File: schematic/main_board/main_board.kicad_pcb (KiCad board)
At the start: 2 copper layers, 13 parts, among them J1 Line OUT, J2 Line IN, P1 +Vref, P2 GND, P3 -Vref, P4 Probe, P5 GND, U1 LM324N

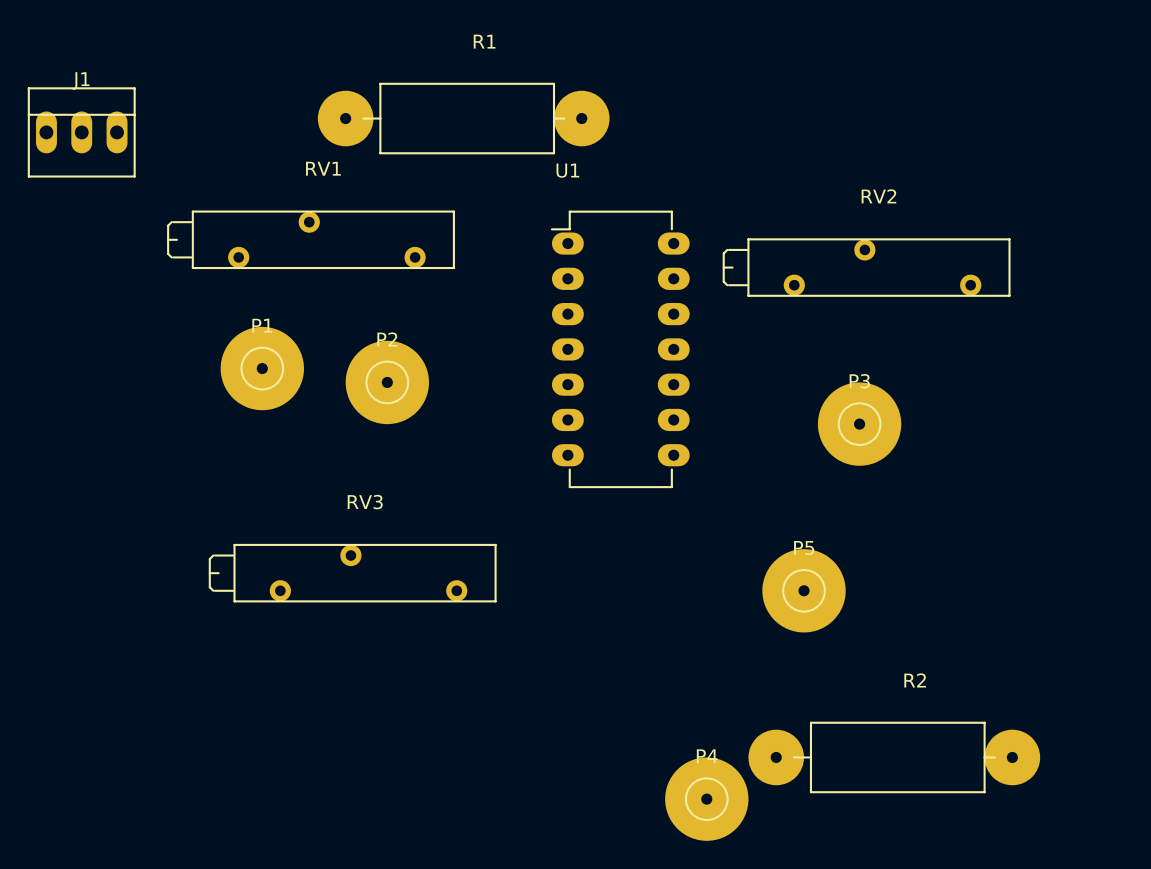
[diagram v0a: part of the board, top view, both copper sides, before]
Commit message: Trace route some wires on PCB.
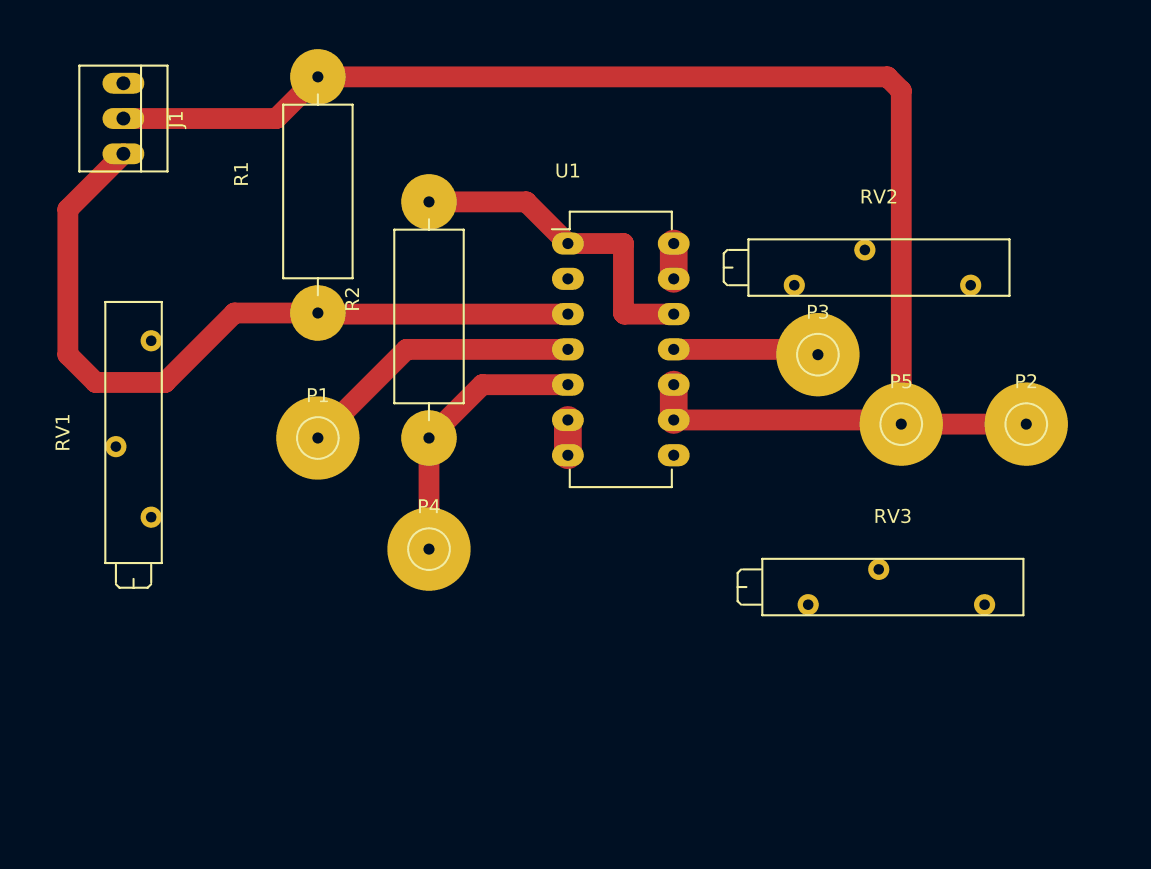
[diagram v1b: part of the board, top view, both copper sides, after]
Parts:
- moved P2 46.1 mm to (181.0, 89.0)
- moved RV3 38.0 mm to (178.0, 102.0)
- moved R2 34.0 mm to (138.0, 90.0), turned to 90 degrees
- moved P4 26.9 mm to (138.0, 98.0)
- moved RV1 19.9 mm to (118.0, 83.0), turned to 90 degrees
- moved R1 14.1 mm to (130.0, 81.0), turned to 90 degrees
- moved P5 13.9 mm to (172.0, 89.0)
- moved P1 6.40 mm to (130.0, 90.0)
- moved P3 5.83 mm to (166.0, 84.0)
- moved J1 3.16 mm to (116.0, 67.0), turned to 270 degrees
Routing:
- net GND: track 0.00 -> 109.7 mm
- net Net-(J1-Pad3): track 0.00 -> 55.0 mm
- net Net-(R2-Pad2): track 0.00 -> 23.9 mm
- net +12V: track 0.00 -> 20.6 mm
- net Net-(P4-Pad1): track 0.00 -> 19.6 mm
- net -12V: track 0.00 -> 10.5 mm
- net Net-(RV2-Pad1): track 0.00 -> 2.54 mm
- net Net-(RV3-Pad1): track 0.00 -> 2.54 mm
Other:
- net class Default: clearance 0.2 -> 0.5; trace_width 0.25 -> 1.5
- rule trace_clearance: 0.2 -> 0.5

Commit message: Add footprint for potentiometer.
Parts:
- RV1, RV2, RV3: footprint Potentiometers:Potentiometer_Bourns_3005_Angular_ScrewFront -> footprints:Potentiometer_CP3-36
- moved RV1 26.5 mm to (123.0, 109.0)
- moved RV2 20.1 mm to (186.0, 61.0)
- moved RV3 10.0 mm to (186.0, 108.0)

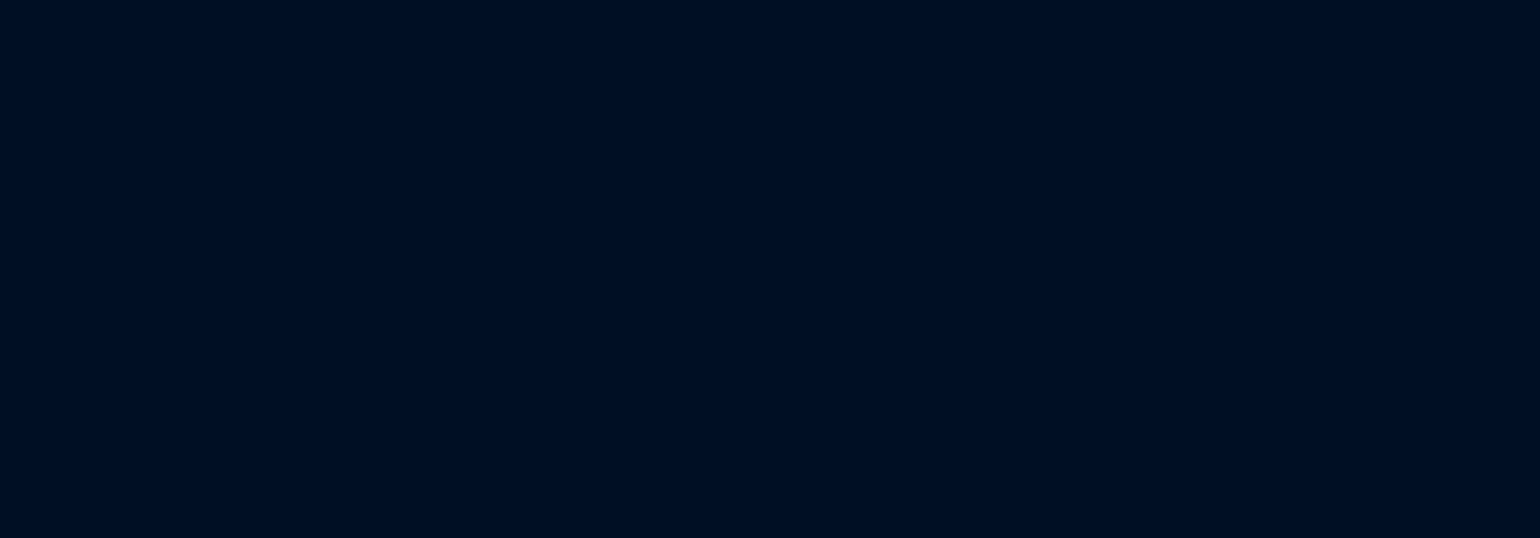
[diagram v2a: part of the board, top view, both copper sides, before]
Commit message: Added circuit to schematic for limit output voltage range.
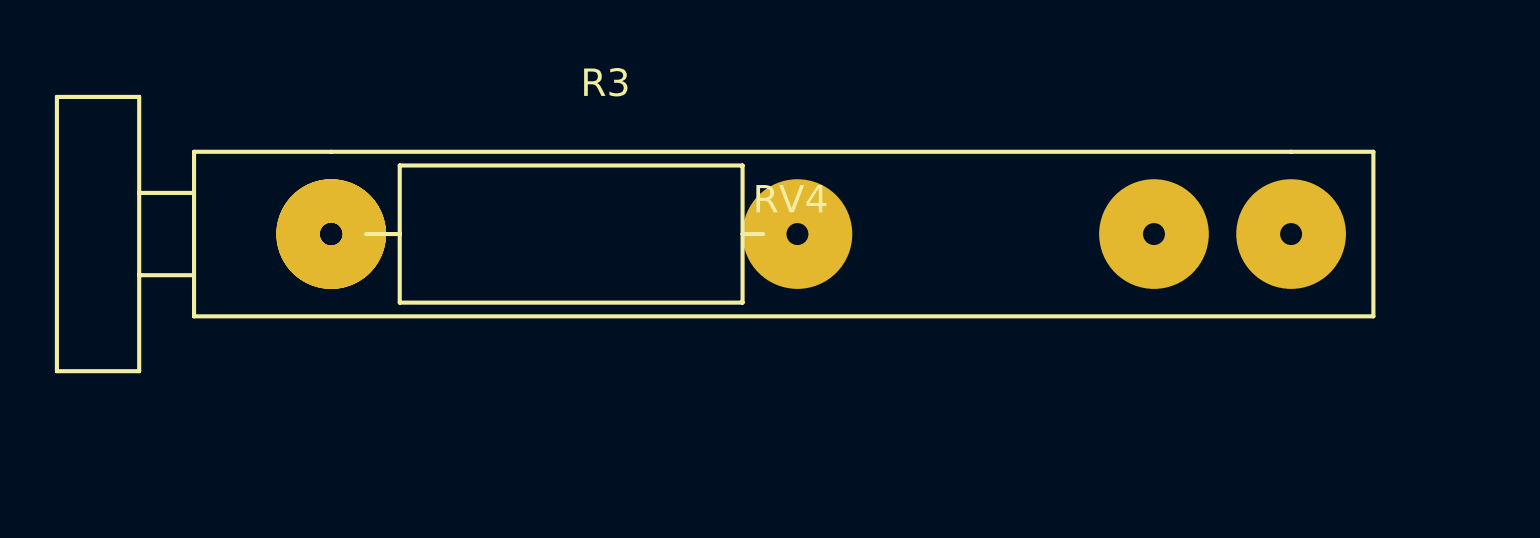
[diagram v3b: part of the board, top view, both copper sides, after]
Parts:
- added R3: 1k, footprints:Resistor_Horizontal_RM20mm_0.25W, F.Cu at (0.00, 0.00)
- added RV4: 100k, footprints:Potentiometer_CP3-36, F.Cu at (0.00, 0.00)
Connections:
- RV2 pad 1: Net-(RV2-Pad1) -> GND
- RV2 pad 3: GND -> Net-(RV2-Pad3)
- RV3 pad 1: Net-(RV3-Pad1) -> GND
- RV3 pad 3: GND -> Net-(RV3-Pad3)
- U1 pad 10: GND -> Net-(J1-Pad3)
- U1 pad 13: Net-(RV2-Pad1) -> Net-(RV2-Pad3)
- U1 pad 14: Net-(RV2-Pad1) -> Net-(RV2-Pad3)
- U1 pad 6: Net-(RV3-Pad1) -> Net-(RV3-Pad3)
- U1 pad 7: Net-(RV3-Pad1) -> Net-(RV3-Pad3)
- U1 pad 9: GND -> Net-(RV4-Pad2)
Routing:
- net GND: track 109.7 -> 91.1 mm
- net Net-(RV4-Pad2): track 0.00 -> 16.1 mm
- net Net-(RV2-Pad3): track 0.00 -> 2.54 mm
- net Net-(RV2-Pad1): track 2.54 -> 0.00 mm
- net Net-(J1-Pad3): track 55.0 -> 57.6 mm
- net Net-(RV3-Pad3): track 0.00 -> 2.54 mm
- net Net-(RV3-Pad1): track 2.54 -> 0.00 mm
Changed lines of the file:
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@@
 (kicad_pcb (version 4) (host pcbnew 4.0.2+e4-6225~38~ubuntu14.04.1-stable)
   (general
-    (links 25)
-    (no_connects 10)
+    (links 27)
+    (no_connects 14)
     (area 0 0 0 0)
     (thickness 1.6)
@@
     (tracks 32)
     (zones 0)
-    (modules 13)
-    (nets 14)
+    (modules 15)
+    (nets 17)
   )
   (page A4)
@@
   (net 9 "Net-(R2-Pad2)")
   (net 10 "Net-(RV1-Pad2)")
-  (net 11 "Net-(RV2-Pad1)")
-  (net 12 "Net-(RV3-Pad1)")
-  (net 13 "Net-(U1-Pad8)")
+  (net 11 "Net-(C1-Pad1)")
+  (net 12 "Net-(D2-Pad2)")
+  (net 13 "Net-(RV2-Pad3)")
+  (net 14 "Net-(RV3-Pad3)")
+  (net 15 "Net-(D1-Pad2)")
+  (net 16 "Net-(RV4-Pad2)")
   (net_class Default "This is the default net class."
     (clearance 0.5)
@@
     (add_net -12V)
     (add_net GND)
+    (add_net "Net-(C1-Pad1)")
+    (add_net "Net-(D1-Pad2)")
+    (add_net "Net-(D2-Pad2)")
     (add_net "Net-(J1-Pad1)")
     (add_net "Net-(J1-Pad3)")
@@
     (add_net "Net-(R2-Pad2)")
     (add_net "Net-(RV1-Pad2)")
-    (add_net "Net-(RV2-Pad1)")
-    (add_net "Net-(RV3-Pad1)")
-    (add_net "Net-(U1-Pad8)")
+    (add_net "Net-(RV2-Pad3)")
+    (add_net "Net-(RV3-Pad3)")
+    (add_net "Net-(RV4-Pad2)")
   )
   (module Connect:PINHEAD1-3 (layer F.Cu)
@@
       (net 8 "Net-(P4-Pad1)"))
     (pad 6 thru_hole oval (at 0 12.7) (size 2.3 1.6) (drill 0.8) (layers *.Cu *.Mask F.SilkS)
-      (net 12 "Net-(RV3-Pad1)"))
+      (net 14 "Net-(RV3-Pad3)"))
     (pad 7 thru_hole oval (at 0 15.24) (size 2.3 1.6) (drill 0.8) (layers *.Cu *.Mask F.SilkS)
-      (net 12 "Net-(RV3-Pad1)"))
+      (net 14 "Net-(RV3-Pad3)"))
     (pad 8 thru_hole oval (at 7.62 15.24) (size 2.3 1.6) (drill 0.8) (layers *.Cu *.Mask F.SilkS)
-      (net 13 "Net-(U1-Pad8)"))
+      (net 15 "Net-(D1-Pad2)"))
     (pad 9 thru_hole oval (at 7.62 12.7) (size 2.3 1.6) (drill 0.8) (layers *.Cu *.Mask F.SilkS)
-      (net 2 GND))
+      (net 16 "Net-(RV4-Pad2)"))
     (pad 10 thru_hole oval (at 7.62 10.16) (size 2.3 1.6) (drill 0.8) (layers *.Cu *.Mask F.SilkS)
-      (net 2 GND))
+      (net 3 "Net-(J1-Pad3)"))
     (pad 11 thru_hole oval (at 7.62 7.62) (size 2.3 1.6) (drill 0.8) (layers *.Cu *.Mask F.SilkS)
       (net 7 -12V))
@@
       (net 9 "Net-(R2-Pad2)"))
     (pad 13 thru_hole oval (at 7.62 2.54) (size 2.3 1.6) (drill 0.8) (layers *.Cu *.Mask F.SilkS)
-      (net 11 "Net-(RV2-Pad1)"))
+      (net 13 "Net-(RV2-Pad3)"))
     (pad 14 thru_hole oval (at 7.62 0) (size 2.3 1.6) (drill 0.8) (layers *.Cu *.Mask F.SilkS)
-      (net 11 "Net-(RV2-Pad1)"))
+      (net 13 "Net-(RV2-Pad3)"))
     (model Housings_DIP.3dshapes/DIP-14_W7.62mm_LongPads.wrl
       (at (xyz 0 0 0))
@@
     (fp_line (start -5 -3) (end 0 -3) (layer F.SilkS) (width 0.15))
     (pad 3 thru_hole circle (at 30 0) (size 4 4) (drill 0.8) (layers *.Cu *.Mask F.SilkS)
-      (net 2 GND))
+      (net 13 "Net-(RV2-Pad3)"))
     (pad 2 thru_hole circle (at 35 0) (size 4 4) (drill 0.8) (layers *.Cu *.Mask F.SilkS)
       (net 4 "Net-(J2-Pad1)"))
     (pad 1 thru_hole circle (at 0 0) (size 4 4) (drill 0.8) (layers *.Cu *.Mask F.SilkS)
-      (net 11 "Net-(RV2-Pad1)"))
+      (net 2 GND))
     (model Potentiometers.3dshapes/Potentiometer_Bourns_3005_Angular_ScrewFront.wrl
       (at (xyz 0 0 0))
@@
     (fp_line (start -5 -3) (end 0 -3) (layer F.SilkS) (width 0.15))
     (pad 3 thru_hole circle (at 30 0) (size 4 4) (drill 0.8) (layers *.Cu *.Mask F.SilkS)
-      (net 2 GND))
+      (net 14 "Net-(RV3-Pad3)"))
     (pad 2 thru_hole circle (at 35 0) (size 4 4) (drill 0.8) (layers *.Cu *.Mask F.SilkS)
       (net 5 "Net-(J2-Pad3)"))
     (pad 1 thru_hole circle (at 0 0) (size 4 4) (drill 0.8) (layers *.Cu *.Mask F.SilkS)
-      (net 12 "Net-(RV3-Pad1)"))
+      (net 2 GND))
+    (model Potentiometers.3dshapes/Potentiometer_Bourns_3005_Angular_ScrewFront.wrl
+      (at (xyz 0 0 0))
+      (scale (xyz 1 1 1))
+      (rotate (xyz 0 0 0))
+    )
+  )
+  (module footprints:Resistor_Horizontal_RM20mm_0.25W (layer F.Cu)
+    (at 0 0)
+    (descr "Resistor, Axial, RM 20mm,")
+    (tags "Resistor Axial RM 20mm")
+    (fp_text reference R3 (at 10 -5.4991) (layer F.SilkS)
+      (effects (font (size 1 1) (thickness 0.15)))
+    )
+    (fp_text value 1k (at 10 5.00126) (layer F.Fab)
+      (effects (font (size 1 1) (thickness 0.15)))
+    )
+    (fp_line (start 15 0) (end 15.75 0) (layer F.SilkS) (width 0.15))
+    (fp_line (start 2.5 0) (end 2.5 -2.5) (layer F.SilkS) (width 0.15))
+    (fp_line (start 2.5 -2.5) (end 15 -2.5) (layer F.SilkS) (width 0.15))
+    (fp_line (start 15 -2.5) (end 15 2.5) (layer F.SilkS) (width 0.15))
+    (fp_line (start 15 2.5) (end 2.5 2.5) (layer F.SilkS) (width 0.15))
+    (fp_line (start 2.5 2.5) (end 2.5 0) (layer F.SilkS) (width 0.15))
+    (fp_line (start 1.27 0) (end 2.38 0) (layer F.SilkS) (width 0.15))
+    (pad 1 thru_hole circle (at 0 0) (size 4 4) (drill 0.8) (layers *.Cu *.SilkS *.Mask)
+      (net 11 "Net-(C1-Pad1)"))
+    (pad 2 thru_hole circle (at 17 0) (size 4 4) (drill 0.8) (layers *.Cu *.SilkS *.Mask)
+      (net 12 "Net-(D2-Pad2)"))
+    (model Resistors_ThroughHole.3dshapes/Resistor_Horizontal_RM20mm.wrl
+      (at (xyz 0.395 0 0))
+      (scale (xyz 0.395 0.4 0.4))
+      (rotate (xyz 0 0 0))
+    )
+  )
+  (module footprints:Potentiometer_CP3-36 (layer F.Cu)
+    (at 0 0)
+    (descr "3/4, Rectangular, Trimpot, Trimming, Potentiometer, Bourns, 3005")
+    (tags "3/4, Rectangular, Trimpot, Trimming, Potentiometer, 3005")
+    (fp_text reference RV4 (at 16.75 -1.25) (layer F.SilkS)
+      (effects (font (size 1 1) (thickness 0.15)))
+    )
+    (fp_text value 100k (at 17 0.75) (layer F.Fab)
+      (effects (font (size 1 1) (thickness 0.15)))
+    )
+    (fp_line (start -7 -1.5) (end -7 -5) (layer F.SilkS) (width 0.15))
+    (fp_line (start -7 -5) (end -10 -5) (layer F.SilkS) (width 0.15))
+    (fp_line (start -10 -5) (end -10 5) (layer F.SilkS) (width 0.15))
+    (fp_line (start -10 5) (end -7 5) (layer F.SilkS) (width 0.15))
+    (fp_line (start -7 5) (end -7 1.5) (layer F.SilkS) (width 0.15))
+    (fp_line (start -5 -1.5) (end -7 -1.5) (layer F.SilkS) (width 0.15))
+    (fp_line (start -7 -1.5) (end -7 1.5) (layer F.SilkS) (width 0.15))
+    (fp_line (start -7 1.5) (end -5 1.5) (layer F.SilkS) (width 0.15))
+    (fp_line (start 0 -3) (end 35 -3) (layer F.SilkS) (width 0.15))
+    (fp_line (start 35 -3) (end 38 -3) (layer F.SilkS) (width 0.15))
+    (fp_line (start 38 -3) (end 38 3) (layer F.SilkS) (width 0.15))
+    (fp_line (start 38 3) (end -5 3) (layer F.SilkS) (width 0.15))
+    (fp_line (start -5 3) (end -5 -3) (layer F.SilkS) (width 0.15))
+    (fp_line (start -5 -3) (end 0 -3) (layer F.SilkS) (width 0.15))
+    (pad 3 thru_hole circle (at 30 0) (size 4 4) (drill 0.8) (layers *.Cu *.Mask F.SilkS)
+      (net 15 "Net-(D1-Pad2)"))
+    (pad 2 thru_hole circle (at 35 0) (size 4 4) (drill 0.8) (layers *.Cu *.Mask F.SilkS)
+      (net 16 "Net-(RV4-Pad2)"))
+    (pad 1 thru_hole circle (at 0 0) (size 4 4) (drill 0.8) (layers *.Cu *.Mask F.SilkS)
+      (net 2 GND))
     (model Potentiometers.3dshapes/Potentiometer_Bourns_3005_Angular_ScrewFront.wrl
       (at (xyz 0 0 0))
@@
   (segment (start 171 64) (end 172 65) (width 1.5) (layer F.Cu) (net 2))
   (segment (start 172 89) (end 181 89) (width 1.5) (layer F.Cu) (net 2))
-  (segment (start 155.62 88.7) (end 171.7 88.7) (width 1.5) (layer F.Cu) (net 2))
   (segment (start 171.7 88.7) (end 172 89) (width 1.5) (layer F.Cu) (net 2))
-  (segment (start 155.62 86.16) (end 155.62 88.7) (width 2) (layer F.Cu) (net 2))
+  (segment (start 155.62 86.16) (end 155.62 88.7) (width 2) (layer F.Cu) (net 3))
   (segment (start 130 81) (end 124 81) (width 1.5) (layer F.Cu) (net 3))
   (segment (start 112 73.54) (end 116 69.54) (width 1.5) (layer F.Cu) (net 3))
@@
   (segment (start 138 73) (end 145 73) (width 1.5) (layer F.Cu) (net 9))
   (segment (start 145 73) (end 148 76) (width 1.5) (layer F.Cu) (net 9))
-  (segment (start 155.62 76) (end 155.62 78.54) (width 2) (layer F.Cu) (net 11))
-  (segment (start 148 88.7) (end 148 91.24) (width 2) (layer F.Cu) (net 12))
+  (segment (start 155.62 76) (end 155.62 78.54) (width 2) (layer F.Cu) (net 13))
+  (segment (start 148 88.7) (end 148 91.24) (width 2) (layer F.Cu) (net 14))
+  (segment (start 155.62 88.7) (end 171.7 88.7) (width 1.5) (layer F.Cu) (net 16))
 )
